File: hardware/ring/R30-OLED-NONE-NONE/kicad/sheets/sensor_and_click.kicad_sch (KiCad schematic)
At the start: 7 parts, among them SW1 5mm 200gf dome, U2 PAW3204DB-TJ3L

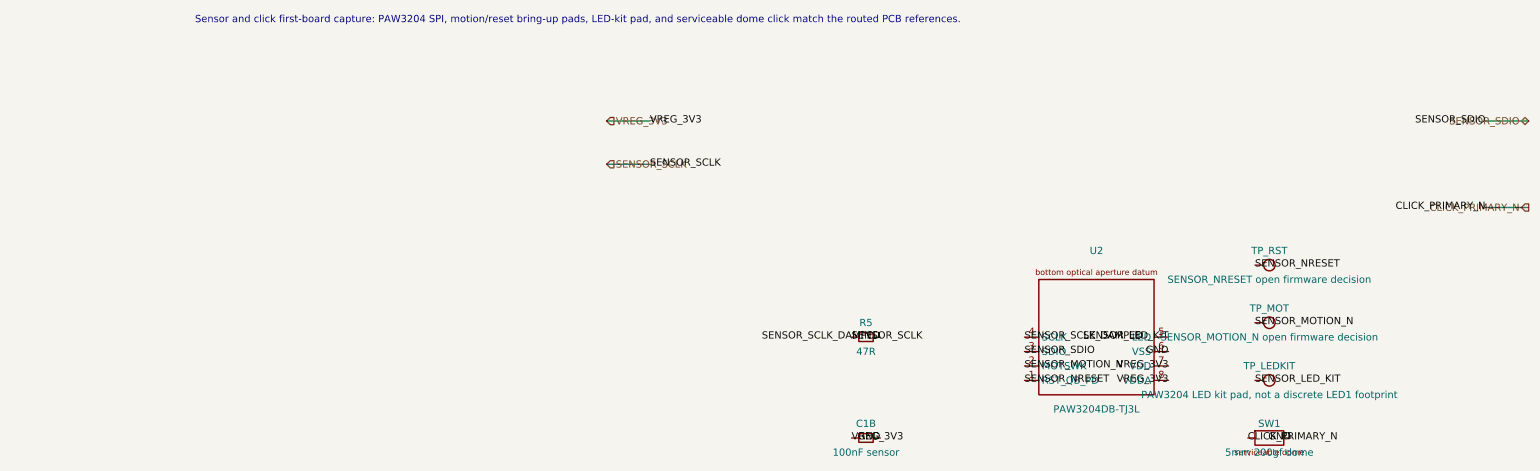
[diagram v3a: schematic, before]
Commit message: fix(r30): reconcile schematic net parity
Sensing mechanism: PAW3204 optical surface tracking.

Form factor and angle: R30 30-degree ring, OLED/NONE/NONE active lane.

Intended use: accessibility-first BLE HID pointing first-board validation.

BOM estimate: active R30 prototype remains about .30-.45, target about .
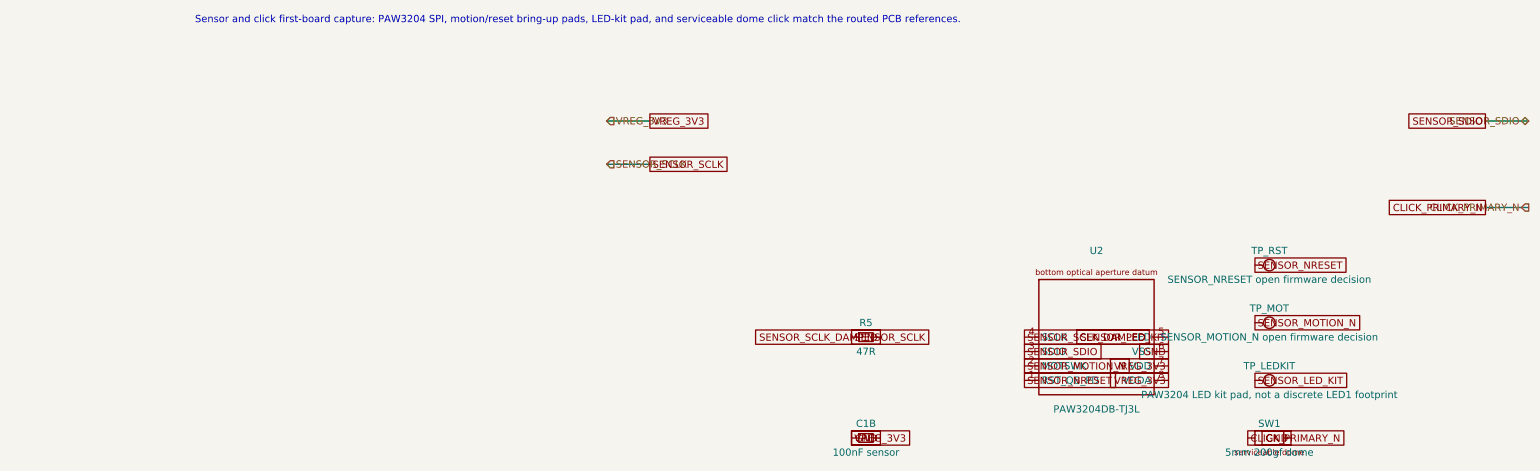
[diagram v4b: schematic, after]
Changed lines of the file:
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@@
     (wire (pts (xy 180.34 38.1) (xy 187.96 38.1)) (stroke (width 0) (type default) (color 0 0 0 0)))
     (wire (pts (xy 180.34 53.34) (xy 187.96 53.34)) (stroke (width 0) (type default) (color 0 0 0 0)))
-  (label "VREG_3V3" (at 33.02 38.1 0) (effects (font (size 1.27 1.27))))
-  (label "SENSOR_SCLK" (at 33.02 45.72 0) (effects (font (size 1.27 1.27))))
-    (label "SENSOR_SDIO" (at 180.34 38.1 180) (effects (font (size 1.27 1.27))))
-    (label "CLICK_PRIMARY_N" (at 180.34 53.34 180) (effects (font (size 1.27 1.27))))
+  (global_label "VREG_3V3" (shape passive) (at 33.02 38.1 0) (effects (font (size 1.27 1.27))))
+  (global_label "SENSOR_SCLK" (shape passive) (at 33.02 45.72 0) (effects (font (size 1.27 1.27))))
+    (global_label "SENSOR_SDIO" (shape passive) (at 180.34 38.1 180) (effects (font (size 1.27 1.27))))
+    (global_label "CLICK_PRIMARY_N" (shape passive) (at 180.34 53.34 180) (effects (font (size 1.27 1.27))))
   (symbol (lib_id "PowerFinger:PAW3204DB-TJ3L_FirstBoard") (at 111.76 76.2 0) (unit 1)
     (in_bom yes) (on_board yes) (dnp no)
@@
     )
   )
-  (label "SENSOR_NRESET" (at 99.06 83.82 0) (effects (font (size 1.27 1.27))))
-  (label "SENSOR_MOTION_N" (at 99.06 81.28 0) (effects (font (size 1.27 1.27))))
-  (label "SENSOR_SDIO" (at 99.06 78.74 0) (effects (font (size 1.27 1.27))))
-  (label "SENSOR_SCLK_DAMPED" (at 99.06 76.2 0) (effects (font (size 1.27 1.27))))
-  (label "SENSOR_LED_KIT" (at 124.46 76.2 180) (effects (font (size 1.27 1.27))))
-  (label "GND" (at 124.46 78.74 180) (effects (font (size 1.27 1.27))))
-  (label "VREG_3V3" (at 124.46 81.28 180) (effects (font (size 1.27 1.27))))
-  (label "VREG_3V3" (at 124.46 83.82 180) (effects (font (size 1.27 1.27))))
-  (label "SENSOR_SCLK" (at 68.58 76.2 0) (effects (font (size 1.27 1.27))))
-  (label "SENSOR_SCLK_DAMPED" (at 73.66 76.2 180) (effects (font (size 1.27 1.27))))
-  (label "VREG_3V3" (at 68.58 93.98 0) (effects (font (size 1.27 1.27))))
-  (label "GND" (at 73.66 93.98 180) (effects (font (size 1.27 1.27))))
-  (label "CLICK_PRIMARY_N" (at 138.43 93.98 0) (effects (font (size 1.27 1.27))))
-  (label "GND" (at 146.05 93.98 180) (effects (font (size 1.27 1.27))))
-  (label "SENSOR_NRESET" (at 139.7 63.5 0) (effects (font (size 1.27 1.27))))
-  (label "SENSOR_MOTION_N" (at 139.7 73.66 0) (effects (font (size 1.27 1.27))))
-  (label "SENSOR_LED_KIT" (at 139.7 83.82 0) (effects (font (size 1.27 1.27))))
+  (global_label "SENSOR_NRESET" (shape passive) (at 99.06 83.82 0) (effects (font (size 1.27 1.27))))
+  (global_label "SENSOR_MOTION_N" (shape passive) (at 99.06 81.28 0) (effects (font (size 1.27 1.27))))
+  (global_label "SENSOR_SDIO" (shape passive) (at 99.06 78.74 0) (effects (font (size 1.27 1.27))))
+  (global_label "SENSOR_SCLK_DAMPED" (shape passive) (at 99.06 76.2 0) (effects (font (size 1.27 1.27))))
+  (global_label "SENSOR_LED_KIT" (shape passive) (at 124.46 76.2 180) (effects (font (size 1.27 1.27))))
+  (global_label "GND" (shape passive) (at 124.46 78.74 180) (effects (font (size 1.27 1.27))))
+  (global_label "VREG_3V3" (shape passive) (at 124.46 81.28 180) (effects (font (size 1.27 1.27))))
+  (global_label "VREG_3V3" (shape passive) (at 124.46 83.82 180) (effects (font (size 1.27 1.27))))
+  (global_label "SENSOR_SCLK" (shape passive) (at 68.58 76.2 0) (effects (font (size 1.27 1.27))))
+  (global_label "SENSOR_SCLK_DAMPED" (shape passive) (at 73.66 76.2 180) (effects (font (size 1.27 1.27))))
+  (global_label "VREG_3V3" (shape passive) (at 68.58 93.98 0) (effects (font (size 1.27 1.27))))
+  (global_label "GND" (shape passive) (at 73.66 93.98 180) (effects (font (size 1.27 1.27))))
+  (global_label "CLICK_PRIMARY_N" (shape passive) (at 138.43 93.98 0) (effects (font (size 1.27 1.27))))
+  (global_label "GND" (shape passive) (at 146.05 93.98 180) (effects (font (size 1.27 1.27))))
+  (global_label "SENSOR_NRESET" (shape passive) (at 139.7 63.5 0) (effects (font (size 1.27 1.27))))
+  (global_label "SENSOR_MOTION_N" (shape passive) (at 139.7 73.66 0) (effects (font (size 1.27 1.27))))
+  (global_label "SENSOR_LED_KIT" (shape passive) (at 139.7 83.82 0) (effects (font (size 1.27 1.27))))
   (sheet_instances
     (path "/" (page "1"))

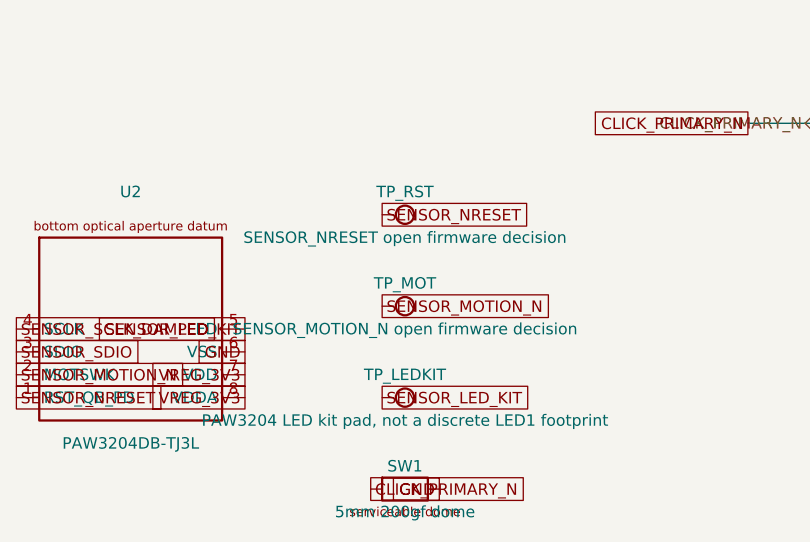
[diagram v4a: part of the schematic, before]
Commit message: fix(r30): reduce active-lane drc debt
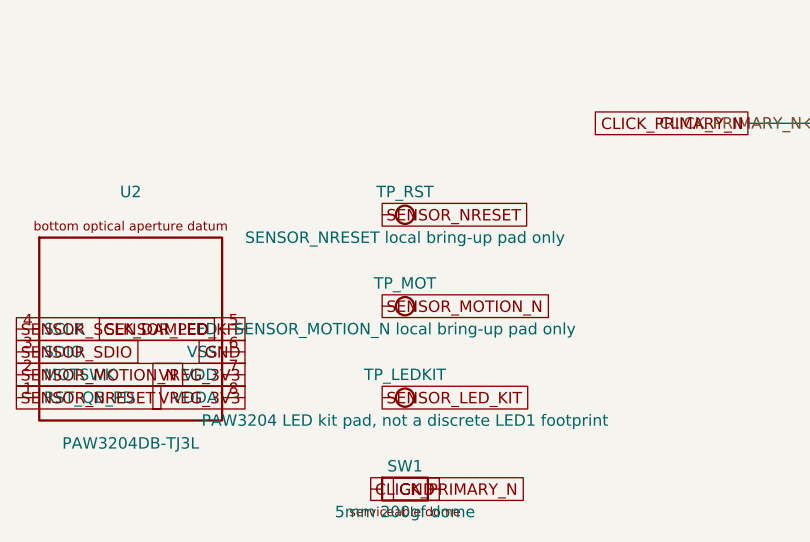
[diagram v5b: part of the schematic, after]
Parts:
- TP_MOT: value SENSOR_MOTION_N open firmware decision -> SENSOR_MOTION_N local bring-up pad only
- TP_RST: value SENSOR_NRESET open firmware decision -> SENSOR_NRESET local bring-up pad only
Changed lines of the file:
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@@
       (effects (font (size 1.27 1.27)))
     )
-    (property "Value" "SENSOR_NRESET open firmware decision" (at 142.24 66.04 0)
+    (property "Value" "SENSOR_NRESET local bring-up pad only" (at 142.24 66.04 0)
       (effects (font (size 1.27 1.27)))
     )
@@
       (effects (font (size 1.27 1.27)))
     )
-    (property "Value" "SENSOR_MOTION_N open firmware decision" (at 142.24 76.2 0)
+    (property "Value" "SENSOR_MOTION_N local bring-up pad only" (at 142.24 76.2 0)
       (effects (font (size 1.27 1.27)))
     )

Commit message: feat(r30): close optical ring fabrication review gate
Sensing mechanism: PAW3204 optical sensor with matched lens/emitter path. Form factor and angle: R30-OLED-NONE-NONE fingertip ring, 30 deg optical posture. Intended use case: offline BLE HID pointing/accessibility ring. BOM estimate: remains under the sub- prototype target in the active R30 BOM.
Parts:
- removed TP_LEDKIT: PAW3204 LED kit pad, not a discrete LED1 footprint, TestPoint:TestPoint_Pad_D1.0mm, symbol PowerFinger:TESTPAD_1MM
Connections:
- net SENSOR_LED_KIT: no longer names the net of U2.5 (LED)
- no-connect marks 0 -> 1
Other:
- note added: "Sensor and click first-board capture: PAW3204 SPI, motion/reset bring-up pads, LED-kit local sensor pin, and serviceable dome click match the routed PCB references."
- note removed: "Sensor and click first-board capture: PAW3204 SPI, motion/reset bring-up pads, LED-kit pad, and serviceable dome click match the routed PCB references."
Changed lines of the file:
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@@
   (generator_version "0.1")
   (paper "A4")
-  (text "Sensor and click first-board capture: PAW3204 SPI, motion/reset bring-up pads, LED-kit pad, and serviceable dome click match the routed PCB references."
+  (text "Sensor and click first-board capture: PAW3204 SPI, motion/reset bring-up pads, LED-kit local sensor pin, and serviceable dome click match the routed PCB references."
     (at 20.32 20.32 0)
     (effects (font (size 1.27 1.27)))
@@
     )
   )
-  (symbol (lib_id "PowerFinger:TESTPAD_1MM") (at 142.24 83.82 0) (unit 1)
-    (in_bom yes) (on_board yes) (dnp no)
-    (property "Reference" "TP_LEDKIT" (at 142.24 81.28 0)
-      (effects (font (size 1.27 1.27)))
-    )
-    (property "Value" "PAW3204 LED kit pad, not a discrete LED1 footprint" (at 142.24 86.36 0)
-      (effects (font (size 1.27 1.27)))
-    )
-    (property "Footprint" "TestPoint:TestPoint_Pad_D1.0mm" (at 142.24 88.9 0)
-      (effects (font (size 1.27 1.27)) hide)
-    )
-    (pin "1")
-    (instances
-      (project "r30_oled_none_none"
-        (path "/" (reference "TP_LEDKIT") (unit 1))
-      )
-    )
-  )
   (global_label "SENSOR_NRESET" (shape passive) (at 99.06 83.82 0) (effects (font (size 1.27 1.27))))
   (global_label "SENSOR_MOTION_N" (shape passive) (at 99.06 81.28 0) (effects (font (size 1.27 1.27))))
   (global_label "SENSOR_SDIO" (shape passive) (at 99.06 78.74 0) (effects (font (size 1.27 1.27))))
   (global_label "SENSOR_SCLK_DAMPED" (shape passive) (at 99.06 76.2 0) (effects (font (size 1.27 1.27))))
-  (global_label "SENSOR_LED_KIT" (shape passive) (at 124.46 76.2 180) (effects (font (size 1.27 1.27))))
+  (no_connect (at 124.46 76.2))
   (global_label "GND" (shape passive) (at 124.46 78.74 180) (effects (font (size 1.27 1.27))))
   (global_label "VREG_3V3" (shape passive) (at 124.46 81.28 180) (effects (font (size 1.27 1.27))))
@@
   (global_label "SENSOR_NRESET" (shape passive) (at 139.7 63.5 0) (effects (font (size 1.27 1.27))))
   (global_label "SENSOR_MOTION_N" (shape passive) (at 139.7 73.66 0) (effects (font (size 1.27 1.27))))
-  (global_label "SENSOR_LED_KIT" (shape passive) (at 139.7 83.82 0) (effects (font (size 1.27 1.27))))
   (sheet_instances
     (path "/" (page "1"))
